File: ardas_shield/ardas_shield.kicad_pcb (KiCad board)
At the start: 2 copper layers, 68.6 x 53.3 mm, 40 parts, among them CON1 SD_Card, IC1 DS1307, P1 CONN_10, P10 CONN_01X03, P2 CONN_8, P3 CONN_8, P4 CONN_ICSP, P5 CONN_6, P6 TTL_COMM, P7 CONN_01X03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

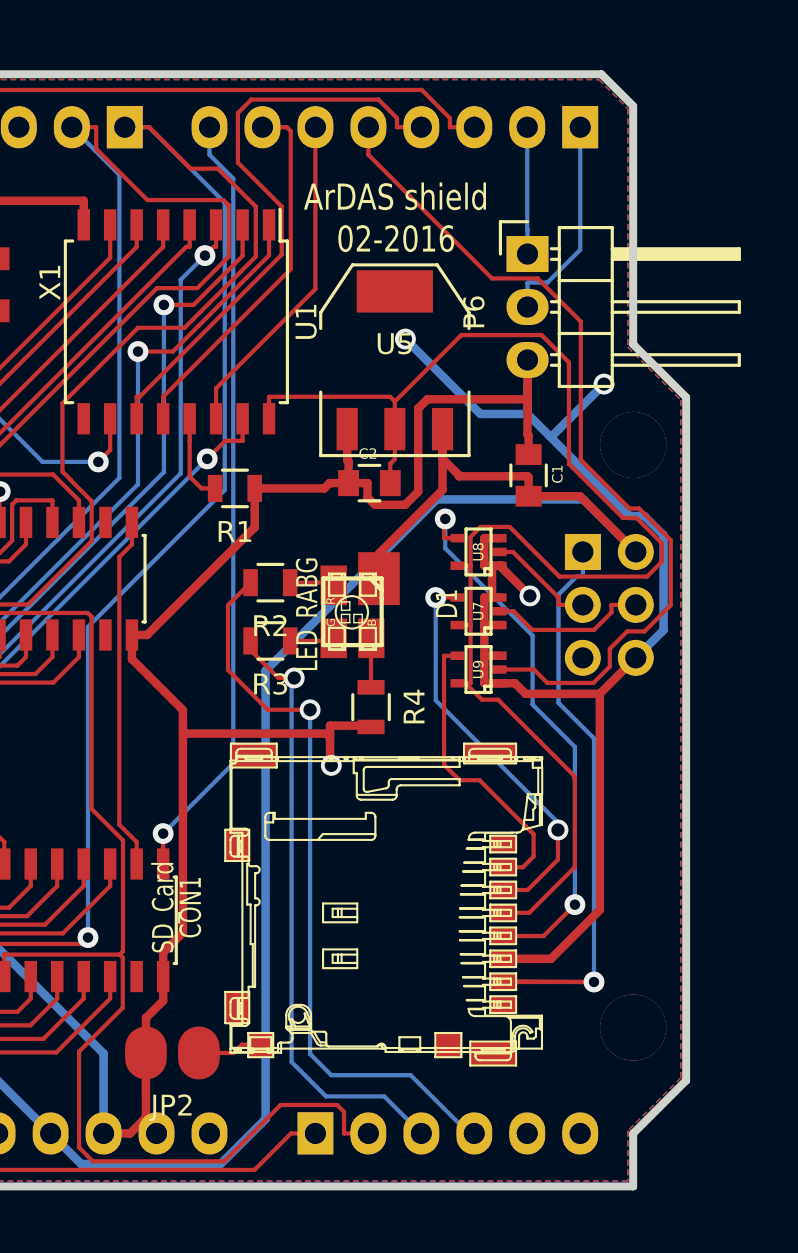
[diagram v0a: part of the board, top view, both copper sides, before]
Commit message: remove sdcard an 5V-3V from PCB
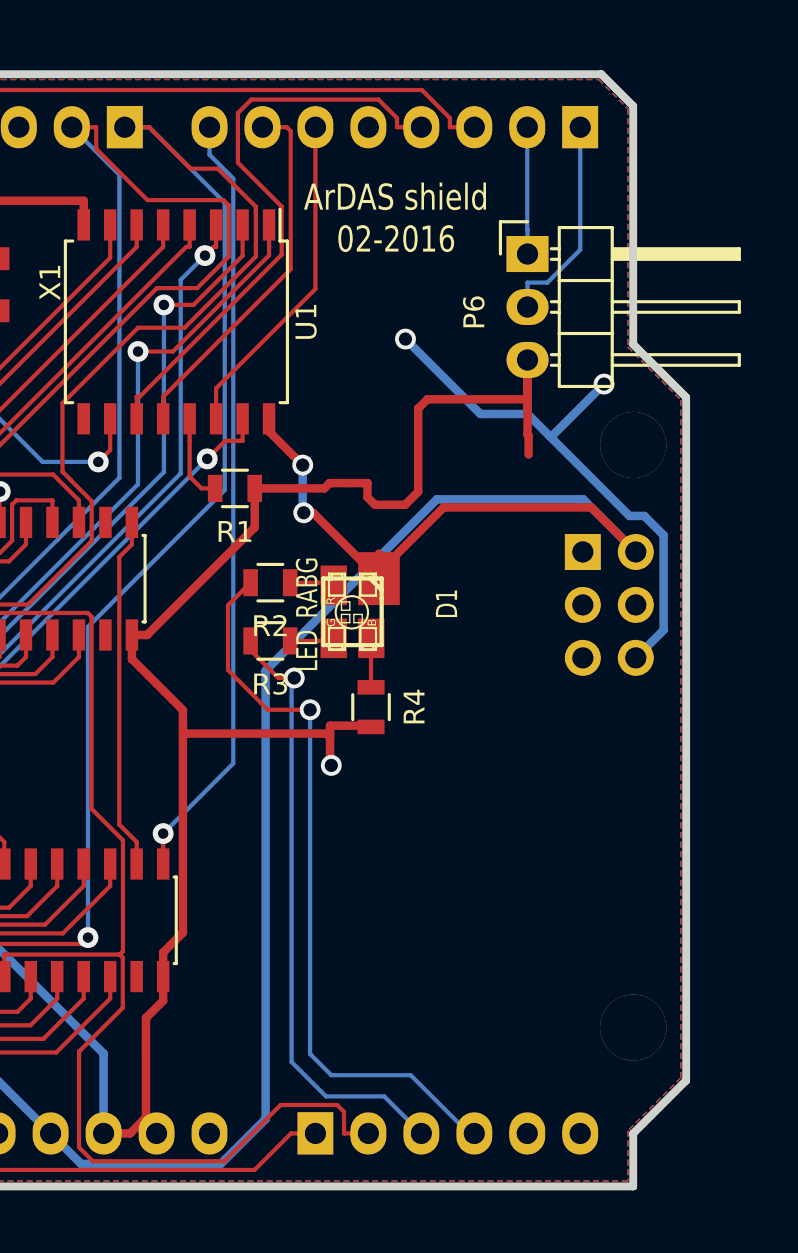
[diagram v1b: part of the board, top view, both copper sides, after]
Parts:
- removed C1, C2: 47uF, kicad-gfa local:C_0805
- removed CON1: SD_Card, kicad-gfa local:microSD_socket
- removed JP2: Jumper_NO_Small, kicad-gfa local:small_no_jumper
- removed U5: LD1117S33TR, kicad-gfa local:SOT-223
- removed U7, U8, U9: 74LVC1G125, kicad-gfa local:SC-70-5
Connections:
- P1 pad 3: (no net) -> Net-(P1-Pad3)
- P1 pad 4: (no net) -> Net-(P1-Pad4)
- P1 pad 5: (no net) -> Net-(P1-Pad5)
- P1 pad 6: (no net) -> Net-(P1-Pad6)
- P1 pad 8: (no net) -> Net-(P1-Pad8)
- P2 pad 1: (no net) -> Net-(P2-Pad1)
- P2 pad 2: (no net) -> Net-(P2-Pad2)
- P2 pad 3: (no net) -> Net-(P2-Pad3)
- P2 pad 4: (no net) -> Net-(P2-Pad4)
- P2 pad 8: (no net) -> Net-(P2-Pad8)
- P3 pad 5: D04 -> Net-(P3-Pad5)
- P4 pad 1: MISO -> Net-(P4-Pad1)
- P4 pad 3: SCK -> Net-(P4-Pad3)
- P4 pad 4: MOSI -> Net-(P4-Pad4)
- P4 pad 5: (no net) -> Net-(P4-Pad5)
- P5 pad 5: (no net) -> Net-(P5-Pad5)
- P5 pad 6: (no net) -> Net-(P5-Pad6)
- U1 pad 16: +3.3V -> +5V
- U1 pad 9: (no net) -> Net-(U1-Pad9)
- U2 pad 7: (no net) -> Net-(U2-Pad7)
- U4 pad 10: (no net) -> Net-(U4-Pad10)
- U4 pad 7: (no net) -> Net-(U4-Pad7)
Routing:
- net +3.3V: track 68.6 -> 0.00 mm
- net D04: track 41.0 -> 0.00 mm
- net GND: track 340.8 -> 301.2 mm, vias 12 -> 11
- net MISO: track 30.7 -> 0.00 mm, vias 1 -> 0
- net /SCK3: track 26.7 -> 0.00 mm, vias 2 -> 0
- net /MOSI3: track 19.3 -> 0.00 mm, vias 2 -> 0
- net /SEN3: track 14.3 -> 0.00 mm
- net MOSI: track 7.61 -> 0.00 mm
- net SCK: track 5.25 -> 0.00 mm
- net +5V: track 239.7 -> 244.6 mm, vias 3 -> 5
- net Net-(CON1-PadCD1): track 3.13 -> 0.00 mm
